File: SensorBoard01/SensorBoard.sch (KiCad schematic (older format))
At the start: 29 parts, among them U1 DS7505, U2 74HC595-PWR

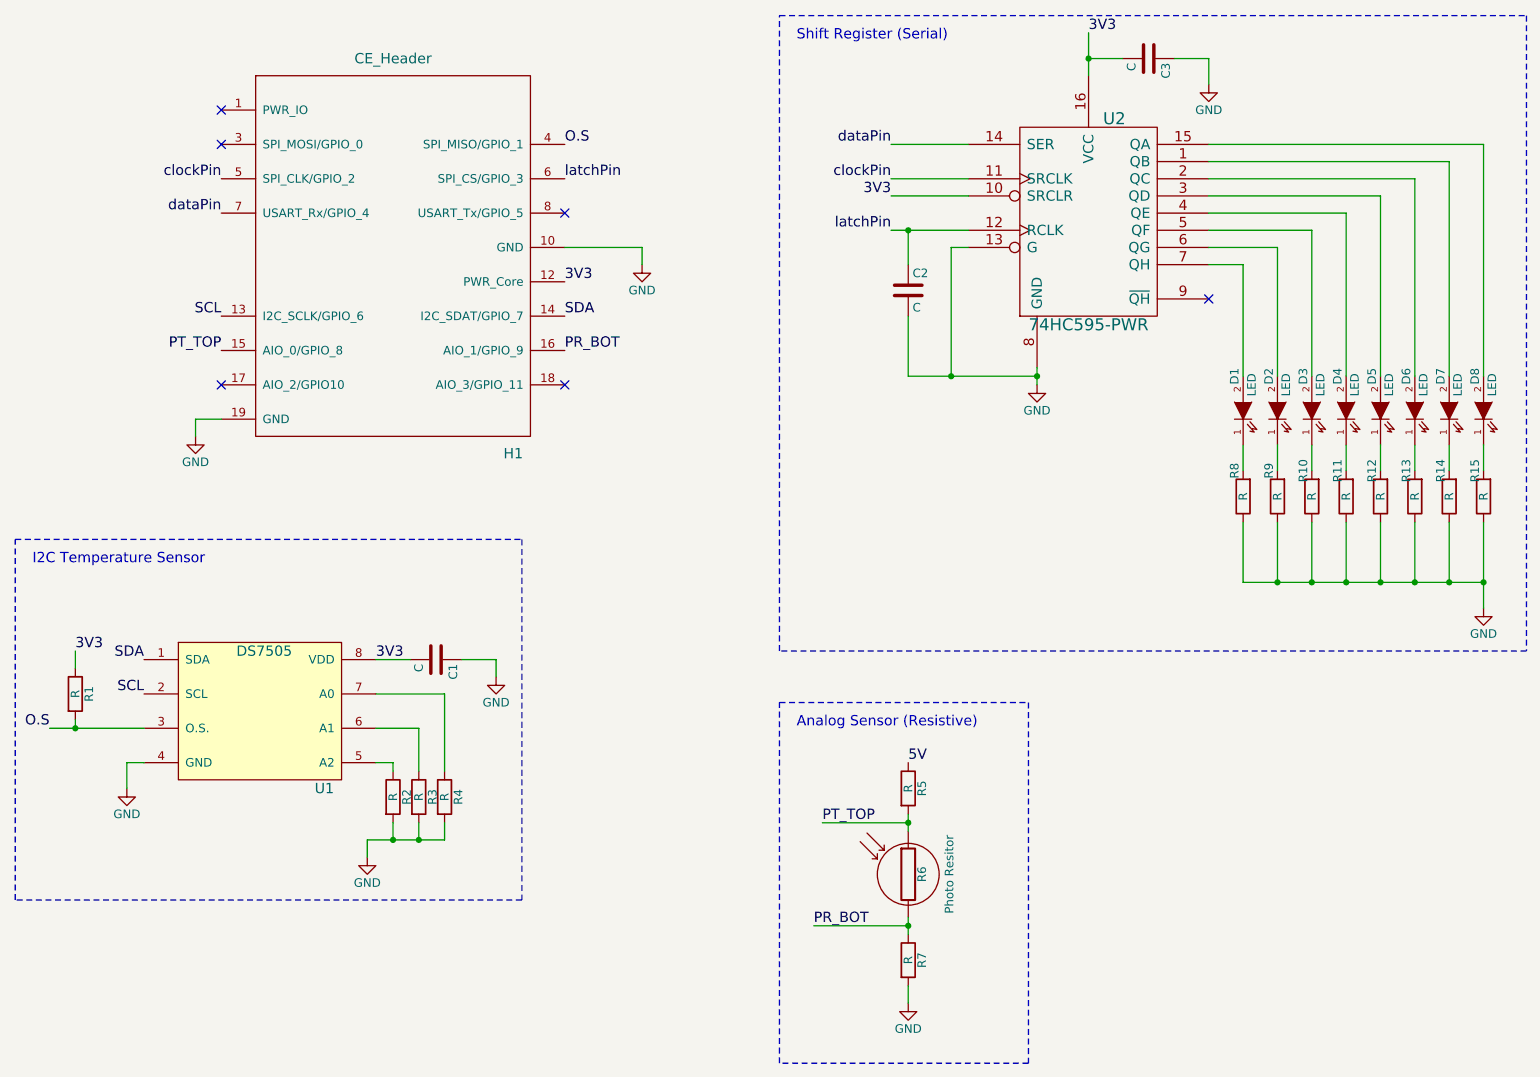
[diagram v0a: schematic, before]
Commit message: Completed the layout for the CE_Header sensor board
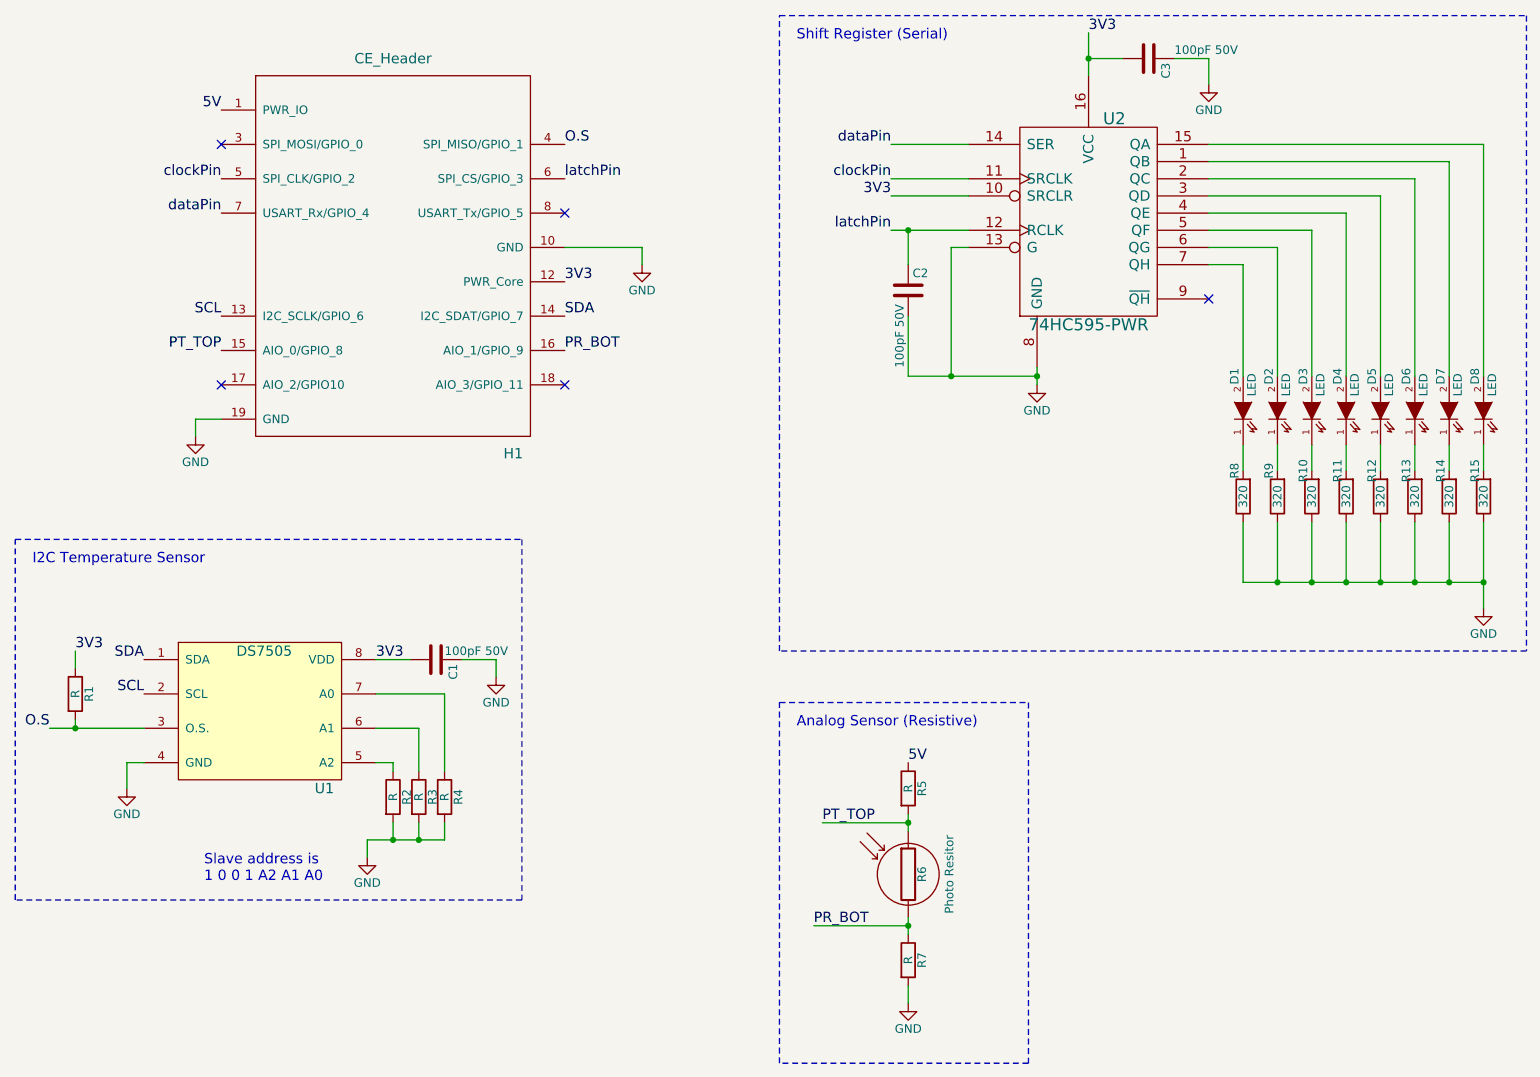
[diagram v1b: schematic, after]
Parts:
- C1, C2, C3: value C -> 100pF 50V
- R10, R11, R12, R13, R14, R15, R8, R9: value R -> 320
- R6: footprint Capacitors_ThroughHole:CP_Radial_Tantal_D5.5mm_P5.00mm -> CE_Header:Photo_Resistor_LDR01; Link Value -> https://www.reichelt.de/Fotodioden-etc-/LDR-07/3/index.html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; MPN PDV-P8103 -> LDR 07
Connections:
- net 5V: now also H1.1 (PWR_IO)
- no-connect marks 6 -> 5
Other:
- note added: "Slave address is \n1 0 0 1 A2 A1 A0\n"
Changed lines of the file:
@@
 P 9300 3550
 F 0 "R15" V 9350 3400 50  0000 C CNN
-F 1 "R" V 9300 3550 50  0000 C CNN
+F 1 "320" V 9300 3550 50  0000 C CNN
 F 2 "Resistors_SMD:R_0805" V 9230 3550 30  0001 C CNN
 F 3 "" H 9300 3550 30  0000 C CNN
@@
 P 9100 3550
 F 0 "R14" V 9150 3400 50  0000 C CNN
-F 1 "R" V 9100 3550 50  0000 C CNN
+F 1 "320" V 9100 3550 50  0000 C CNN
 F 2 "Resistors_SMD:R_0805" V 9030 3550 30  0001 C CNN
 F 3 "" H 9100 3550 30  0000 C CNN
@@
 P 8900 3550
 F 0 "R13" V 8950 3400 50  0000 C CNN
-F 1 "R" V 8900 3550 50  0000 C CNN
+F 1 "320" V 8900 3550 50  0000 C CNN
 F 2 "Resistors_SMD:R_0805" V 8830 3550 30  0001 C CNN
 F 3 "" H 8900 3550 30  0000 C CNN
@@
 P 8700 3550
 F 0 "R12" V 8750 3400 50  0000 C CNN
-F 1 "R" V 8700 3550 50  0000 C CNN
+F 1 "320" V 8700 3550 50  0000 C CNN
 F 2 "Resistors_SMD:R_0805" V 8630 3550 30  0001 C CNN
 F 3 "" H 8700 3550 30  0000 C CNN
@@
 P 8500 3550
 F 0 "R11" V 8550 3400 50  0000 C CNN
-F 1 "R" V 8500 3550 50  0000 C CNN
+F 1 "320" V 8500 3550 50  0000 C CNN
 F 2 "Resistors_SMD:R_0805" V 8430 3550 30  0001 C CNN
 F 3 "" H 8500 3550 30  0000 C CNN
@@
 P 8300 3550
 F 0 "R10" V 8350 3400 50  0000 C CNN
-F 1 "R" V 8300 3550 50  0000 C CNN
+F 1 "320" V 8300 3550 50  0000 C CNN
 F 2 "Resistors_SMD:R_0805" V 8230 3550 30  0001 C CNN
 F 3 "" H 8300 3550 30  0000 C CNN
@@
 P 8100 3550
 F 0 "R9" V 8150 3400 50  0000 C CNN
-F 1 "R" V 8100 3550 50  0000 C CNN
+F 1 "320" V 8100 3550 50  0000 C CNN
 F 2 "Resistors_SMD:R_0805" V 8030 3550 30  0001 C CNN
 F 3 "" H 8100 3550 30  0000 C CNN
@@
 P 7900 3550
 F 0 "R8" V 7950 3400 50  0000 C CNN
-F 1 "R" V 7900 3550 50  0000 C CNN
+F 1 "320" V 7900 3550 50  0000 C CNN
 F 2 "Resistors_SMD:R_0805" V 7830 3550 30  0001 C CNN
 F 3 "" H 7900 3550 30  0000 C CNN
@@
 F 0 "R6" V 6030 5750 50  0000 C CNN
 F 1 "Photo Resitor" V 6160 5750 50  0000 C TNN
-F 2 "Capacitors_ThroughHole:CP_Radial_Tantal_D5.5mm_P5.00mm" V 5880 5750 30  0001 C CNN
+F 2 "CE_Header:Photo_Resistor_LDR01" V 5880 5750 30  0001 C CNN
 F 3 "" H 5950 5750 30  0000 C CNN
-F 4 "PDV-P8103" H 5950 5750 60  0001 C CNN "MPN"
-F 5 "Value" H 5950 5750 60  0001 C CNN "Link"
+F 4 "LDR 07" H 5950 5750 60  0001 C CNN "MPN"
+F 5 "https://www.reichelt.de/Fotodioden-etc-/LDR-07/3/index.html?ACTION=3&LA=446&ARTICLE=10208&GROUPID=3045&artnr=LDR+07&SEARCH=fotowiderstand" H 5950 5750 60  0001 C CNN "Link"
 	1    5950 5750
 	1    0    0    -1
@@
 	9300 1500 9300 2850
 Wire Wire Line
-	9300 3700 9300 4050
-Wire Wire Line
-	9300 4050 9300 4200
+	9300 3700 9300 4200
 Wire Wire Line
 	9100 3250 9100 3400
@@
 	7900 3700 7900 4050
 Wire Wire Line
-	7900 4050 8100 4050
-Wire Wire Line
-	8100 4050 8300 4050
-Wire Wire Line
-	8300 4050 8500 4050
-Wire Wire Line
-	8500 4050 8700 4050
-Wire Wire Line
-	8700 4050 8900 4050
-Wire Wire Line
-	8900 4050 9100 4050
-Wire Wire Line
-	9100 4050 9300 4050
+	7900 4050 9300 4050
 Connection ~ 8100 4050
 Connection ~ 8300 4050
@@
 	3250 5550 3250 5450
 Wire Wire Line
-	2800 5550 2950 5550
-Wire Wire Line
-	2950 5550 3100 5550
-Wire Wire Line
-	3100 5550 3250 5550
+	2800 5550 3250 5550
 Wire Wire Line
 	2800 5550 2800 5650
@@
 Connection ~ 3100 5550
 Wire Wire Line
-	950  4900 1100 4900
-Wire Wire Line
-	1100 4900 1500 4900
+	950  4900 1500 4900
 Wire Wire Line
 	1100 4900 1100 4850
@@
 	1100 4550 1100 4450
 Wire Wire Line
-	5950 5400 5950 5450
-Wire Wire Line
-	5950 5450 5950 5500
-Wire Wire Line
-	5950 6000 5950 6050
-Wire Wire Line
-	5950 6050 5950 6100
+	5950 5400 5950 5500
+Wire Wire Line
+	5950 6000 5950 6100
 Wire Wire Line
 	5950 6400 5950 6500
@@
 Connection ~ 5950 6050
 Wire Wire Line
-	6700 2800 6700 2850
-Wire Wire Line
-	6700 2850 6700 2900
+	6700 2800 6700 2900
 Wire Wire Line
 	6300 2100 6200 2100
 Wire Wire Line
-	5950 2850 6200 2850
-Wire Wire Line
-	6200 2850 6700 2850
+	5950 2850 6700 2850
 Connection ~ 6700 2850
 Wire Wire Line
@@
 	6300 1800 5850 1800
 Wire Wire Line
-	5850 2000 5950 2000
-Wire Wire Line
-	5950 2000 6300 2000
+	5850 2000 6300 2000
 Wire Wire Line
 	7700 2200 7900 2200
@@
 P 5950 2350
 F 0 "C2" H 5975 2450 50  0000 L CNN
-F 1 "C" H 5975 2250 50  0000 L CNN
+F 1 "100pF 50V" V 5900 1900 50  0000 L CNN
 F 2 "Capacitors_SMD:C_0805" H 5988 2200 30  0001 C CNN
 F 3 "" H 5950 2350 60  0000 C CNN
@@
 P 7350 1000
 F 0 "C3" H 7375 1100 50  0000 L CNN
-F 1 "C" H 7375 900 50  0000 L CNN
+F 1 "100pF 50V" V 7300 1150 50  0000 L CNN
 F 2 "Capacitors_SMD:C_0805" H 7388 850 30  0001 C CNN
 F 3 "" H 7350 1000 60  0000 C CNN
@@
 Connection ~ 6200 2850
 Wire Wire Line
-	7000 850  7000 1000
-Wire Wire Line
-	7000 1000 7000 1100
+	7000 850  7000 1100
 Wire Wire Line
 	7000 1000 7200 1000
@@
 P 3200 4500
 F 0 "C1" H 3225 4600 50  0000 L CNN
-F 1 "C" H 3225 4400 50  0000 L CNN
+F 1 "100pF 50V" V 3150 4550 50  0000 L CNN
 F 2 "Capacitors_SMD:C_0805" H 3238 4350 30  0001 C CNN
 F 3 "" H 3200 4500 60  0000 C CNN
@@
 NoConn ~ 1950 2900
 NoConn ~ 1950 1500
-NoConn ~ 1950 1300
 Text Notes 5300 900  0    60   ~ 0
 Shift Register (Serial)
+Text Label 1950 1300 2    60   ~ 0
+5V
+Text Notes 1850 5800 0    60   ~ 0
+Slave address is \n1 0 0 1 A2 A1 A0\n
 $EndSCHEMATC

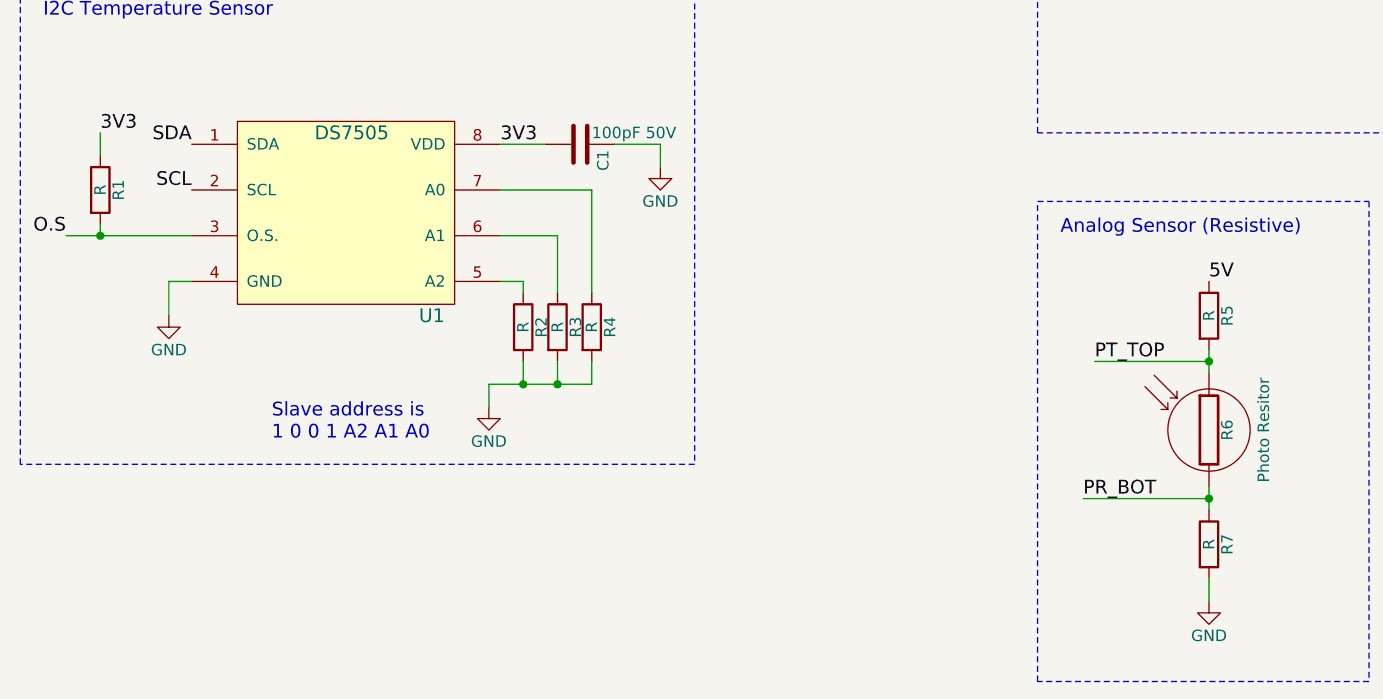
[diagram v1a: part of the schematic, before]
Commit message: Correction to footprint and resistor values
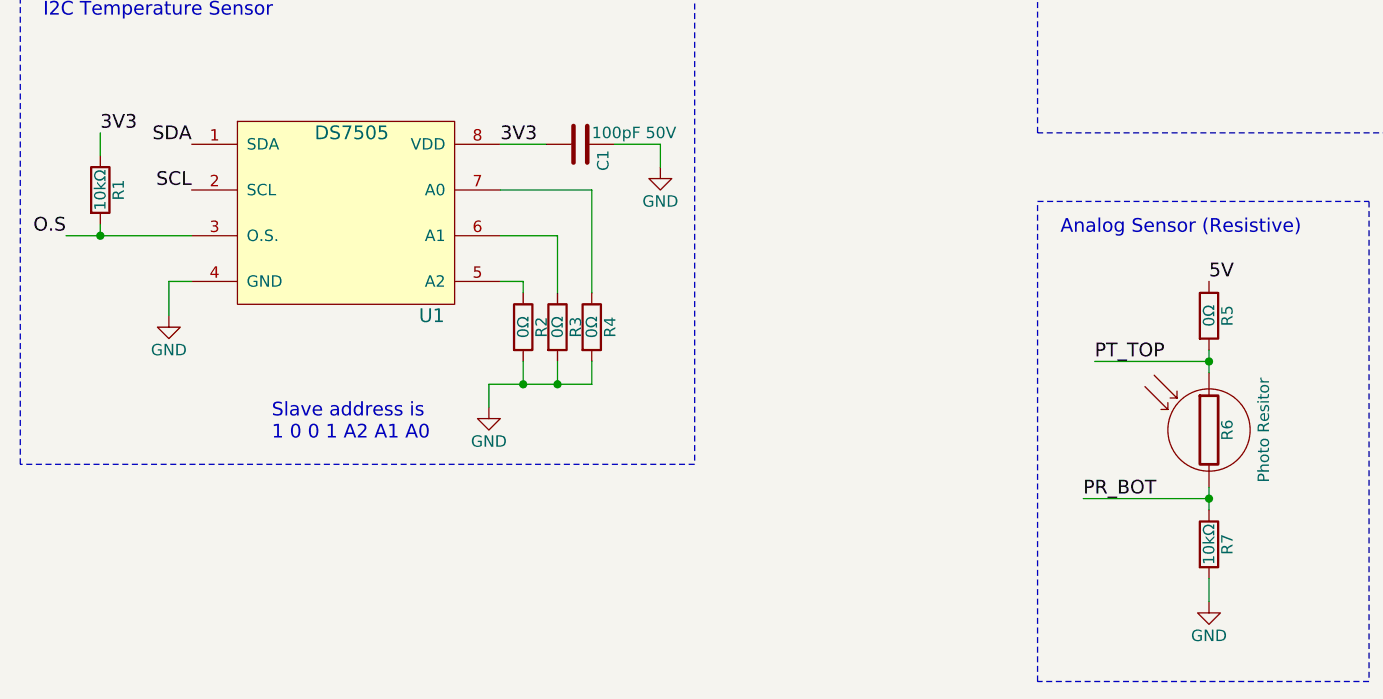
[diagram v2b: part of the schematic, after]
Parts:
- R1, R7: value R -> 10kΩ
- R2, R3, R4, R5: value R -> 0Ω
- U1: footprint Housings_SOIC:SOIC-8-1EP_3.9x4.9mm_Pitch1.27mm -> Housings_SOIC:SOIC-8_3.9x4.9mm_Pitch1.27mm
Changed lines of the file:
@@
 P 5950 5250
 F 0 "R5" V 6030 5250 50  0000 C CNN
-F 1 "R" V 5950 5250 50  0000 C CNN
+F 1 "0Ω" V 5950 5250 50  0000 C CNN
 F 2 "Resistors_SMD:R_0805" V 5880 5250 30  0001 C CNN
 F 3 "" H 5950 5250 30  0000 C CNN
@@
 F 0 "U1" H 2550 4350 60  0000 C CNN
 F 1 "DS7505" H 2200 5150 60  0000 C CNN
-F 2 "Housings_SOIC:SOIC-8-1EP_3.9x4.9mm_Pitch1.27mm" H 2200 4600 60  0001 C CNN
+F 2 "Housings_SOIC:SOIC-8_3.9x4.9mm_Pitch1.27mm" H 2200 4600 60  0001 C CNN
 F 3 "" H 2200 4600 60  0000 C CNN
 	1    2200 4800
@@
 P 2950 5300
 F 0 "R2" V 3030 5300 50  0000 C CNN
-F 1 "R" V 2950 5300 50  0000 C CNN
+F 1 "0Ω" V 2950 5300 50  0000 C CNN
 F 2 "Resistors_SMD:R_0805" V 2880 5300 30  0001 C CNN
 F 3 "" H 2950 5300 30  0000 C CNN
@@
 P 3100 5300
 F 0 "R3" V 3180 5300 50  0000 C CNN
-F 1 "R" V 3100 5300 50  0000 C CNN
+F 1 "0Ω" V 3100 5300 50  0000 C CNN
 F 2 "Resistors_SMD:R_0805" V 3030 5300 30  0001 C CNN
 F 3 "" H 3100 5300 30  0000 C CNN
@@
 P 3250 5300
 F 0 "R4" V 3330 5300 50  0000 C CNN
-F 1 "R" V 3250 5300 50  0000 C CNN
+F 1 "0Ω" V 3250 5300 50  0000 C CNN
 F 2 "Resistors_SMD:R_0805" V 3180 5300 30  0001 C CNN
 F 3 "" H 3250 5300 30  0000 C CNN
@@
 P 1100 4700
 F 0 "R1" V 1180 4700 50  0000 C CNN
-F 1 "R" V 1100 4700 50  0000 C CNN
+F 1 "10kΩ" V 1100 4700 50  0000 C CNN
 F 2 "Resistors_SMD:R_0805" V 1030 4700 30  0001 C CNN
 F 3 "" H 1100 4700 30  0000 C CNN
@@
 P 5950 6250
 F 0 "R7" V 6030 6250 50  0000 C CNN
-F 1 "R" V 5950 6250 50  0000 C CNN
+F 1 "10kΩ" V 5950 6250 50  0000 C CNN
 F 2 "Resistors_SMD:R_0805" V 5880 6250 30  0001 C CNN
 F 3 "" H 5950 6250 30  0000 C CNN

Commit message: A change of mind on the LDR resistor divider
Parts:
- R5: value 0Ω -> 10kΩ
- R7: value 10kΩ -> 0Ω
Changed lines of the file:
@@
 P 5950 5250
 F 0 "R5" V 6030 5250 50  0000 C CNN
-F 1 "0Ω" V 5950 5250 50  0000 C CNN
+F 1 "10kΩ" V 5950 5250 50  0000 C CNN
 F 2 "Resistors_SMD:R_0805" V 5880 5250 30  0001 C CNN
 F 3 "" H 5950 5250 30  0000 C CNN
@@
 P 5950 6250
 F 0 "R7" V 6030 6250 50  0000 C CNN
-F 1 "10kΩ" V 5950 6250 50  0000 C CNN
+F 1 "0Ω" V 5950 6250 50  0000 C CNN
 F 2 "Resistors_SMD:R_0805" V 5880 6250 30  0001 C CNN
 F 3 "" H 5950 6250 30  0000 C CNN

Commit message: Corrected some library reference issues
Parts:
- D1, D2, D3, D4, D5, D6, D7, D8: symbol LED -> LED-RESCUE-SensorBoard
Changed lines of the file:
@@
 EESchema Schematic File Version 2
 LIBS:ce_header
+LIBS:SensorBoard-rescue
 LIBS:power
 LIBS:device
@@
 $EndComp
 $Comp
-L LED D8
+L LED-RESCUE-SensorBoard D8
 U 1 1 58F371C8
 P 9300 3050
@@
 $EndComp
 $Comp
-L LED D7
+L LED-RESCUE-SensorBoard D7
 U 1 1 58F375DE
 P 9100 3050
@@
 $EndComp
 $Comp
-L LED D6
+L LED-RESCUE-SensorBoard D6
 U 1 1 58F376B0
 P 8900 3050
@@
 $EndComp
 $Comp
-L LED D5
+L LED-RESCUE-SensorBoard D5
 U 1 1 58F376BF
 P 8700 3050
@@
 $EndComp
 $Comp
-L LED D4
+L LED-RESCUE-SensorBoard D4
 U 1 1 58F3780A
 P 8500 3050
@@
 $EndComp
 $Comp
-L LED D3
+L LED-RESCUE-SensorBoard D3
 U 1 1 58F37819
 P 8300 3050
@@
 $EndComp
 $Comp
-L LED D2
+L LED-RESCUE-SensorBoard D2
 U 1 1 58F37828
 P 8100 3050
@@
 $EndComp
 $Comp
-L LED D1
+L LED-RESCUE-SensorBoard D1
 U 1 1 58F37837
 P 7900 3050
